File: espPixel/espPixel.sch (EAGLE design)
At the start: 66 parts, among them IC1 74LVC1T45GW,125, IC3 MP2315GJ-Z, IC4 CP2104, J1 TBLH10-350-04BK, J2 TBLH10-350-03BK, J3 TBLH10-350-02BK, Q1 SIR414DP-T1-GE3, Q2 SIR414DP-T1-GE3, Q5 mmbt2222, Q6 mmbt2222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

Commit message: bug fix
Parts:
- L1: value 4uh -> 1.5uh
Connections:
- removed net N$7: C6.2, D1.A, U$1.PVDD, U$1.VDD
- new net VDD: C6.2, D1.A, R12.1, U$1.PVDD, U$1.VDD
- net VIN: no longer R12.1
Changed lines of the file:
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@@
 <setting verticaltext="up"/>
 </settings>
-<grid distance="0.1" unitdist="inch" unit="inch" style="lines" multiple="1" display="no" altdistance="0.01" altunitdist="inch" altunit="inch"/>
+<grid distance="0.05" unitdist="inch" unit="inch" style="lines" multiple="1" display="no" altdistance="0.01" altunitdist="inch" altunit="inch"/>
 <layers>
 <layer number="1" name="Top" color="4" fill="1" visible="no" active="no"/>
@@
 <parts>
 <part name="U$1" library="MIC2101" deviceset="MIC2101" device="QFN16" package3d_urn="urn:adsk.eagle:package:21055/1"/>
-<part name="L1" library="rcl" library_urn="urn:adsk.eagle:library:334" deviceset="L-EU" device="CEP125" package3d_urn="urn:adsk.eagle:package:25968/1" value="4uh"/>
+<part name="L1" library="rcl" library_urn="urn:adsk.eagle:library:334" deviceset="L-EU" device="CEP125" package3d_urn="urn:adsk.eagle:package:25968/1" value="1.5uh"/>
 <part name="Q2" library="SIR414DP-T1-GE3" deviceset="SIR414DP-T1-GE3" device=""/>
 <part name="IC1" library="74LVC1T45GW_125" deviceset="74LVC1T45GW,125" device=""/>
@@
 <pinref part="R11" gate="G$1" pin="1"/>
 <junction x="18.542" y="-46.736"/>
-<pinref part="R12" gate="G$1" pin="1"/>
-<wire x1="18.542" y1="-39.116" x2="18.542" y2="-46.736" width="0.1524" layer="91"/>
 <pinref part="R15" gate="G$1" pin="1"/>
 <wire x1="43.942" y1="-49.276" x2="43.942" y2="-46.736" width="0.1524" layer="91"/>
@@
 <wire x1="92.202" y1="-77.216" x2="92.202" y2="-74.676" width="0.1524" layer="91"/>
 <junction x="92.202" y="-77.216"/>
-</segment>
-</net>
-<net name="N$7" class="0">
-<segment>
-<pinref part="U$1" gate="G$1" pin="PVDD"/>
-<pinref part="U$1" gate="G$1" pin="VDD"/>
-<wire x1="43.942" y1="-69.596" x2="43.942" y2="-72.136" width="0.1524" layer="91"/>
-<pinref part="C6" gate="G$1" pin="2"/>
-<wire x1="41.402" y1="-74.676" x2="43.942" y2="-74.676" width="0.1524" layer="91"/>
-<wire x1="43.942" y1="-74.676" x2="43.942" y2="-72.136" width="0.1524" layer="91"/>
-<junction x="43.942" y="-72.136"/>
-<pinref part="D1" gate="G$1" pin="A"/>
-<wire x1="54.102" y1="-79.756" x2="54.102" y2="-72.136" width="0.1524" layer="91"/>
-<wire x1="54.102" y1="-72.136" x2="43.942" y2="-72.136" width="0.1524" layer="91"/>
 </segment>
 </net>
@@
 </segment>
 </net>
+<net name="VDD" class="0">
+<segment>
+<pinref part="R12" gate="G$1" pin="1"/>
+<wire x1="18.542" y1="-39.116" x2="21.59" y2="-39.116" width="0.1524" layer="91"/>
+<wire x1="21.59" y1="-39.116" x2="21.59" y2="-39.37" width="0.1524" layer="91"/>
+<label x="19.05" y="-38.1" size="1.778" layer="95"/>
+</segment>
+<segment>
+<pinref part="U$1" gate="G$1" pin="PVDD"/>
+<pinref part="U$1" gate="G$1" pin="VDD"/>
+<wire x1="43.942" y1="-69.596" x2="43.942" y2="-72.136" width="0.1524" layer="91"/>
+<pinref part="C6" gate="G$1" pin="2"/>
+<wire x1="41.402" y1="-74.676" x2="43.942" y2="-74.676" width="0.1524" layer="91"/>
+<wire x1="43.942" y1="-74.676" x2="43.942" y2="-72.136" width="0.1524" layer="91"/>
+<junction x="43.942" y="-72.136"/>
+<pinref part="D1" gate="G$1" pin="A"/>
+<wire x1="54.102" y1="-79.756" x2="54.102" y2="-72.136" width="0.1524" layer="91"/>
+<wire x1="54.102" y1="-72.136" x2="43.942" y2="-72.136" width="0.1524" layer="91"/>
+<label x="48.26" y="-72.39" size="1.778" layer="95"/>
+</segment>
+</net>

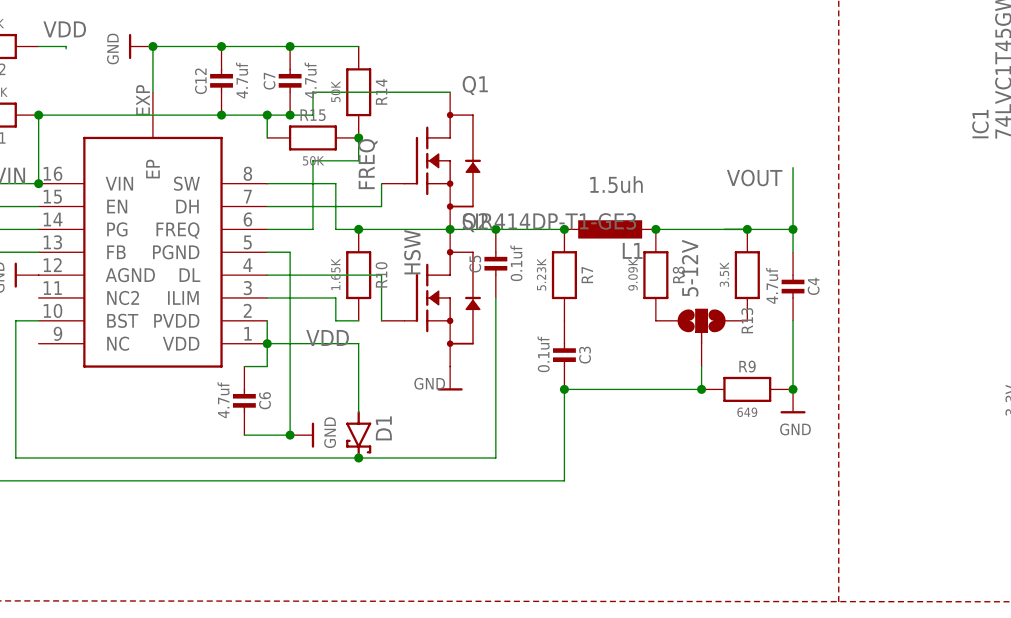
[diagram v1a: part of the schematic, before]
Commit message: Text clean up
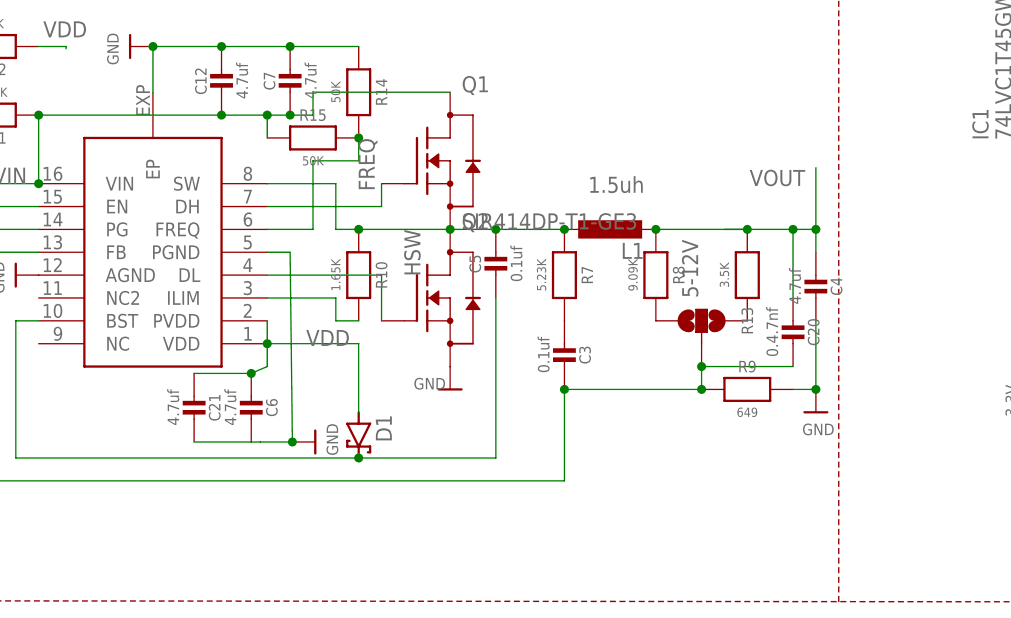
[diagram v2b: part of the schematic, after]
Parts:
- added C20: 0.4.7nf, microbuilder:CAP_CERAMIC0603_NO
- added C21: 4.7uf, microbuilder:CAP_CERAMIC0603_NO
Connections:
- net GND: now also C21.1
- net N$11: now also C20.1
- net VDD: now also C21.2
- net VOUT: now also C20.2
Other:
- moved on the sheet: C4, C6

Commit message: tunining
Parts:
- C20: value 0.4.7nf -> 4.7nf
- L1: value 1.5uh -> 4.7uh
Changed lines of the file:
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@@
 <grid distance="0.01" unitdist="inch" unit="inch" style="lines" multiple="1" display="no" altdistance="0.01" altunitdist="inch" altunit="inch"/>
 <layers>
-<layer number="1" name="Top" color="4" fill="1" visible="yes" active="no"/>
-<layer number="16" name="Bottom" color="1" fill="1" visible="yes" active="no"/>
-<layer number="17" name="Pads" color="2" fill="1" visible="yes" active="no"/>
-<layer number="18" name="Vias" color="2" fill="1" visible="yes" active="no"/>
-<layer number="19" name="Unrouted" color="6" fill="1" visible="yes" active="no"/>
-<layer number="20" name="Dimension" color="24" fill="1" visible="yes" active="no"/>
-<layer number="21" name="tPlace" color="7" fill="1" visible="yes" active="no"/>
-<layer number="22" name="bPlace" color="7" fill="1" visible="yes" active="no"/>
-<layer number="23" name="tOrigins" color="15" fill="1" visible="yes" active="no"/>
-<layer number="24" name="bOrigins" color="15" fill="1" visible="yes" active="no"/>
-<layer number="25" name="tNames" color="7" fill="1" visible="yes" active="no"/>
-<layer number="26" name="bNames" color="7" fill="1" visible="yes" active="no"/>
-<layer number="27" name="tValues" color="7" fill="1" visible="yes" active="no"/>
-<layer number="28" name="bValues" color="7" fill="1" visible="yes" active="no"/>
+<layer number="1" name="Top" color="4" fill="1" visible="no" active="no"/>
+<layer number="16" name="Bottom" color="1" fill="1" visible="no" active="no"/>
+<layer number="17" name="Pads" color="2" fill="1" visible="no" active="no"/>
+<layer number="18" name="Vias" color="2" fill="1" visible="no" active="no"/>
+<layer number="19" name="Unrouted" color="6" fill="1" visible="no" active="no"/>
+<layer number="20" name="Dimension" color="24" fill="1" visible="no" active="no"/>
+<layer number="21" name="tPlace" color="7" fill="1" visible="no" active="no"/>
+<layer number="22" name="bPlace" color="7" fill="1" visible="no" active="no"/>
+<layer number="23" name="tOrigins" color="15" fill="1" visible="no" active="no"/>
+<layer number="24" name="bOrigins" color="15" fill="1" visible="no" active="no"/>
+<layer number="25" name="tNames" color="7" fill="1" visible="no" active="no"/>
+<layer number="26" name="bNames" color="7" fill="1" visible="no" active="no"/>
+<layer number="27" name="tValues" color="7" fill="1" visible="no" active="no"/>
+<layer number="28" name="bValues" color="7" fill="1" visible="no" active="no"/>
 <layer number="29" name="tStop" color="7" fill="3" visible="no" active="no"/>
 <layer number="30" name="bStop" color="7" fill="6" visible="no" active="no"/>
@@
 <layer number="35" name="tGlue" color="7" fill="4" visible="no" active="no"/>
 <layer number="36" name="bGlue" color="7" fill="5" visible="no" active="no"/>
-<layer number="37" name="tTest" color="7" fill="1" visible="yes" active="no"/>
-<layer number="38" name="bTest" color="7" fill="1" visible="yes" active="no"/>
+<layer number="37" name="tTest" color="7" fill="1" visible="no" active="no"/>
+<layer number="38" name="bTest" color="7" fill="1" visible="no" active="no"/>
 <layer number="39" name="tKeepout" color="4" fill="11" visible="no" active="no"/>
 <layer number="40" name="bKeepout" color="1" fill="11" visible="no" active="no"/>
@@
 <layer number="44" name="Drills" color="7" fill="1" visible="no" active="no"/>
 <layer number="45" name="Holes" color="7" fill="1" visible="no" active="no"/>
-<layer number="46" name="Milling" color="3" fill="1" visible="yes" active="no"/>
-<layer number="47" name="Measures" color="7" fill="1" visible="yes" active="no"/>
-<layer number="48" name="Document" color="7" fill="1" visible="yes" active="no"/>
-<layer number="49" name="Reference" color="7" fill="1" visible="yes" active="no"/>
-<layer number="50" name="dxf" color="7" fill="1" visible="yes" active="no"/>
-<layer number="51" name="tDocu" color="7" fill="1" visible="yes" active="no"/>
-<layer number="52" name="bDocu" color="7" fill="1" visible="yes" active="no"/>
-<layer number="53" name="tGND_GNDA" color="7" fill="9" visible="yes" active="no"/>
-<layer number="54" name="bGND_GNDA" color="1" fill="9" visible="yes" active="no"/>
-<layer number="56" name="wert" color="7" fill="1" visible="yes" active="no"/>
-<layer number="57" name="tCAD" color="7" fill="1" visible="yes" active="no"/>
-<layer number="58" name="bCAD" color="11" fill="1" visible="yes" active="no"/>
-<layer number="59" name="tCarbon" color="7" fill="1" visible="yes" active="no"/>
-<layer number="60" name="bCarbon" color="7" fill="1" visible="yes" active="no"/>
+<layer number="46" name="Milling" color="3" fill="1" visible="no" active="no"/>
+<layer number="47" name="Measures" color="7" fill="1" visible="no" active="no"/>
+<layer number="48" name="Document" color="7" fill="1" visible="no" active="no"/>
+<layer number="49" name="Reference" color="7" fill="1" visible="no" active="no"/>
+<layer number="50" name="dxf" color="7" fill="1" visible="no" active="no"/>
+<layer number="51" name="tDocu" color="7" fill="1" visible="no" active="no"/>
+<layer number="52" name="bDocu" color="7" fill="1" visible="no" active="no"/>
+<layer number="53" name="tGND_GNDA" color="7" fill="9" visible="no" active="no"/>
+<layer number="54" name="bGND_GNDA" color="1" fill="9" visible="no" active="no"/>
+<layer number="56" name="wert" color="7" fill="1" visible="no" active="no"/>
+<layer number="57" name="tCAD" color="7" fill="1" visible="no" active="no"/>
+<layer number="58" name="bCAD" color="11" fill="1" visible="no" active="no"/>
+<layer number="59" name="tCarbon" color="7" fill="1" visible="no" active="no"/>
+<layer number="60" name="bCarbon" color="7" fill="1" visible="no" active="no"/>
 <layer number="88" name="SimResults" color="9" fill="1" visible="yes" active="yes"/>
 <layer number="89" name="SimProbes" color="9" fill="1" visible="yes" active="yes"/>
@@
 <parts>
 <part name="U$1" library="MIC2101" deviceset="MIC2101" device="QFN16" package3d_urn="urn:adsk.eagle:package:21055/1"/>
-<part name="L1" library="rcl" library_urn="urn:adsk.eagle:library:334" deviceset="L-EU" device="CEP125" package3d_urn="urn:adsk.eagle:package:25968/1" value="1.5uh"/>
+<part name="L1" library="rcl" library_urn="urn:adsk.eagle:library:334" deviceset="L-EU" device="CEP125" package3d_urn="urn:adsk.eagle:package:25968/1" value="4.7uh"/>
 <part name="Q2" library="SIR414DP-T1-GE3" deviceset="SIR414DP-T1-GE3" device=""/>
 <part name="IC1" library="74LVC1T45GW_125" deviceset="74LVC1T45GW,125" device=""/>
@@
 <part name="RST" library="TL1015AF160QG" deviceset="TL1015AF160QG" device=""/>
 <part name="IO0" library="TL1015AF160QG" deviceset="TL1015AF160QG" device=""/>
-<part name="C20" library="microbuilder" deviceset="CAP_CERAMIC" device="0603_NO" value="0.4.7nf"/>
+<part name="C20" library="microbuilder" deviceset="CAP_CERAMIC" device="0603_NO" value="4.7nf"/>
 <part name="C21" library="microbuilder" deviceset="CAP_CERAMIC" device="0603_NO" value="4.7uf"/>
 </parts>

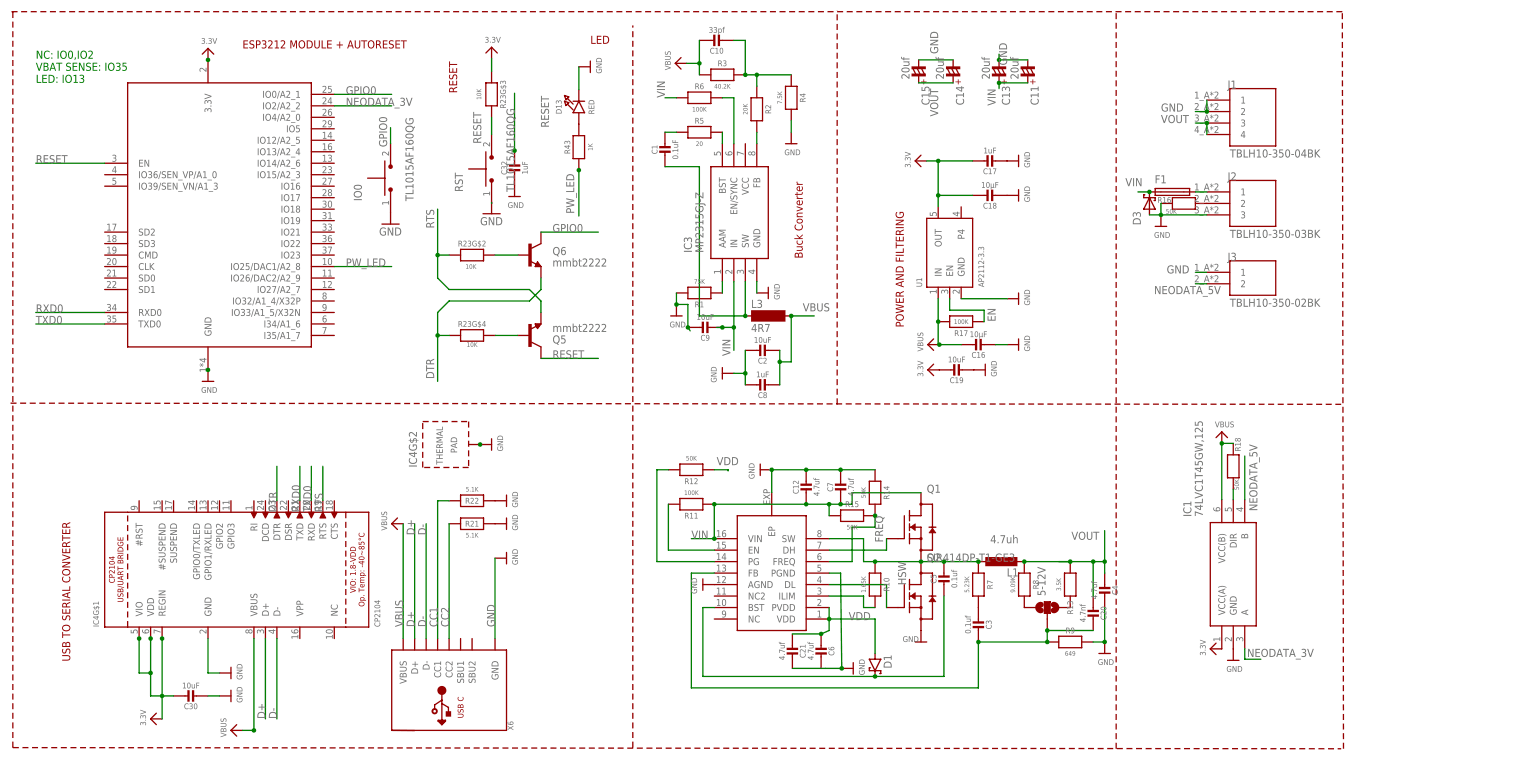
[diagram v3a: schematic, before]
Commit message: ability to turn off the output
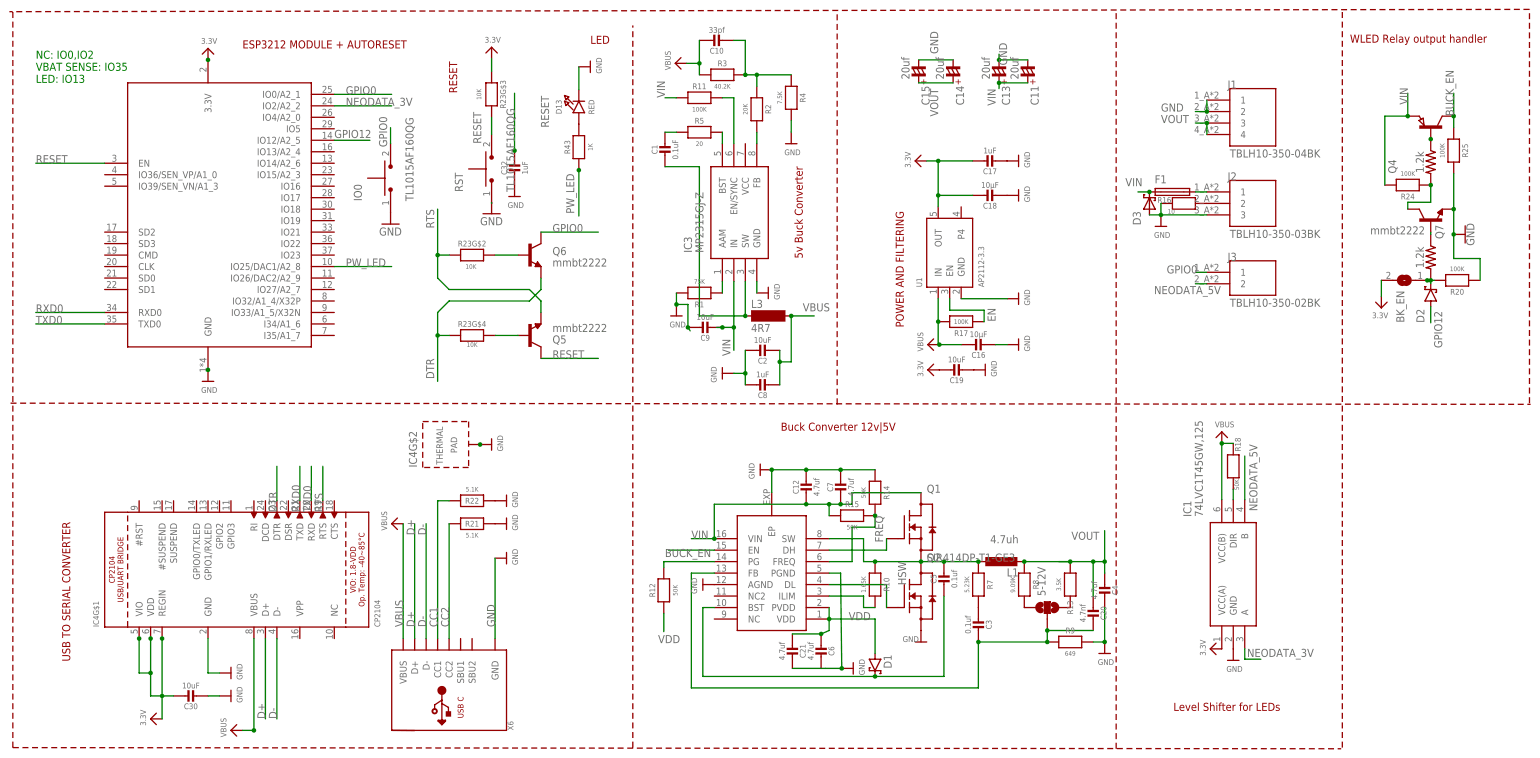
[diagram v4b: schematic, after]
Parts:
- added BK_EN: (no value), jumper:SJ
- added D2: BAT60J, diode:BAT60J
- added Q4: (no value), semicon-smd-ipc:PNP-TRANSISTOR_SOT23
- added Q7: mmbt2222, SparkFun:TRANSISTOR_NPNSOT23-3
- added R19: 1.2k, SparkFun-Resistors:RESISTOR0603
- added R20, R24, R25: 100K, microbuilder:RESISTOR_0603_NOOUT
- R16: value 50K -> 10
- R6: value 100K -> 1.2k; device microbuilder:RESISTOR_0603_NOOUT -> SparkFun-Resistors:RESISTOR0603
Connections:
- removed net N$16: R11.2, U$1.EN
- new net BUCK_EN: Q4.C, R25.1, U$1.EN
- new net GPIO12: D2.A, X8.IO12/A2_5
- new net N$23: Q7.B, R6.1
- new net N$24: Q4.B, R19.1
- new net N$26: Q7.C, R19.2, R24.1
- new net N$9: BK_EN.1, D2.C, R20.2, R6.2
- net 3.3V: now also BK_EN.2
- net GND: now also Q7.E, R20.1, R25.2; no longer J3.1
- net GPIO0: now also J3.1
- net N$5: now also R11.2; no longer R6.2
- net VIN: now also Q4.E, R24.2; no longer R6.1
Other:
- note added: "5v Buck Converter"
- note added: "Buck Converter 12v|5V"
- note added: "Level Shifter for LEDs"
- note added: "WLED Relay output handler"
- note removed: "Buck Converter"
- moved on the sheet: R11, R12
